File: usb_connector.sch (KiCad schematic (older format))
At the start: 7 parts

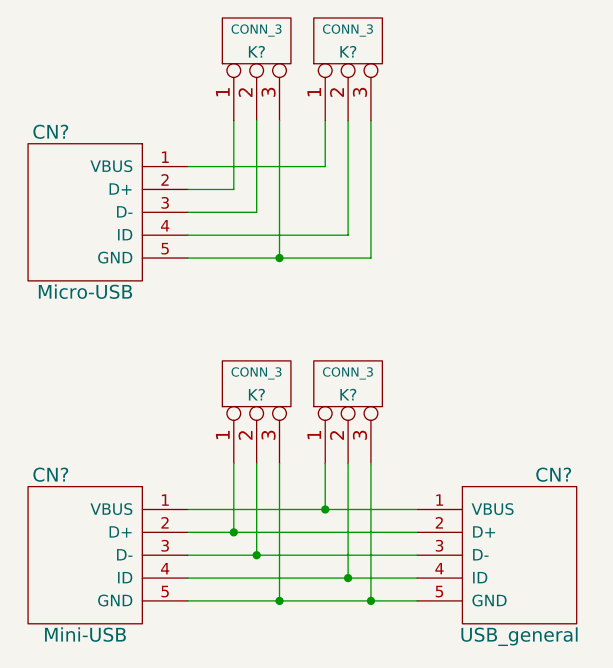
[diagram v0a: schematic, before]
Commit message: Add annotations to parts
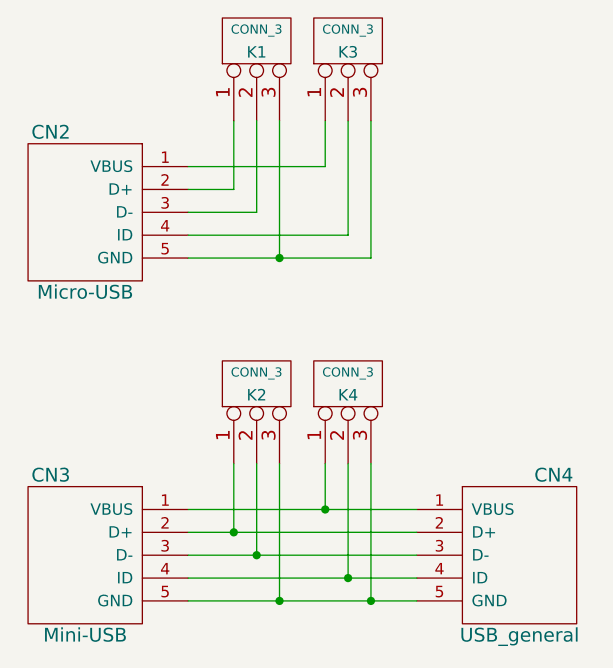
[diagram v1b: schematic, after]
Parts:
- gave numbers to parts that had none: 7
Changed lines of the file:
@@
 $EndDescr
 $Comp
-L USB_general CN?
+L USB_general CN3
 U 1 1 54E6FAE7
 P 3950 4750
-F 0 "CN?" H 3800 5100 60  0000 C CNN
+F 0 "CN3" H 3800 5100 60  0000 C CNN
 F 1 "Mini-USB" H 3950 4400 60  0000 C CNN
 F 2 "" H 4000 4650 60  0000 C CNN
@@
 $EndComp
 $Comp
-L USB_general CN?
+L USB_general CN2
 U 1 1 54E6FAEE
 P 3950 3250
-F 0 "CN?" H 3800 3600 60  0000 C CNN
+F 0 "CN2" H 3800 3600 60  0000 C CNN
 F 1 "Micro-USB" H 3950 2900 60  0000 C CNN
 F 2 "" H 4000 3150 60  0000 C CNN
@@
 	4400 4950 5400 4950
 $Comp
-L USB_general CN?
+L USB_general CN4
 U 1 1 54E6FAFA
 P 5850 4750
-F 0 "CN?" H 5700 5100 60  0000 C CNN
+F 0 "CN4" H 5700 5100 60  0000 C CNN
 F 1 "USB_general" H 5850 4400 60  0000 C CNN
 F 2 "" H 5900 4650 60  0000 C CNN
@@
 $EndComp
 $Comp
-L CONN_3 K?
+L CONN_3 K1
 U 1 1 54E6FB01
 P 4700 2500
-F 0 "K?" V 4650 2500 50  0000 C CNN
+F 0 "K1" V 4650 2500 50  0000 C CNN
 F 1 "CONN_3" V 4750 2500 40  0000 C CNN
 F 2 "" H 4700 2500 60  0000 C CNN
@@
 $EndComp
 $Comp
-L CONN_3 K?
+L CONN_3 K3
 U 1 1 54E6FB08
 P 5100 2500
-F 0 "K?" V 5050 2500 50  0000 C CNN
+F 0 "K3" V 5050 2500 50  0000 C CNN
 F 1 "CONN_3" V 5150 2500 40  0000 C CNN
 F 2 "" H 5100 2500 60  0000 C CNN
@@
 $EndComp
 $Comp
-L CONN_3 K?
+L CONN_3 K2
 U 1 1 54E6FB0F
 P 4700 4000
-F 0 "K?" V 4650 4000 50  0000 C CNN
+F 0 "K2" V 4650 4000 50  0000 C CNN
 F 1 "CONN_3" V 4750 4000 40  0000 C CNN
 F 2 "" H 4700 4000 60  0000 C CNN
@@
 $EndComp
 $Comp
-L CONN_3 K?
+L CONN_3 K4
 U 1 1 54E6FB16
 P 5100 4000
-F 0 "K?" V 5050 4000 50  0000 C CNN
+F 0 "K4" V 5050 4000 50  0000 C CNN
 F 1 "CONN_3" V 5150 4000 40  0000 C CNN
 F 2 "" H 5100 4000 60  0000 C CNN

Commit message: WT12 breakout headers are now in place
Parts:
- CN4: footprint (none) -> replacement_kinesis_controller:Pin_Header_Staggered_Straight_1x05
- K1, K2, K3, K4: footprint (none) -> replacement_kinesis_controller:Pin_Header_Staggered_Straight_1x03
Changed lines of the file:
@@
 F 0 "CN3" H 3800 5100 60  0000 C CNN
 F 1 "Mini-USB" H 3950 4400 60  0000 C CNN
-F 2 "" H 4000 4650 60  0000 C CNN
+F 2 "" H 4000 4650 60  0001 C CNN
 F 3 "" H 4000 4650 60  0000 C CNN
 	1    3950 4750
@@
 F 0 "CN2" H 3800 3600 60  0000 C CNN
 F 1 "Micro-USB" H 3950 2900 60  0000 C CNN
-F 2 "" H 4000 3150 60  0000 C CNN
+F 2 "" H 4000 3150 60  0001 C CNN
 F 3 "" H 4000 3150 60  0000 C CNN
 	1    3950 3250
@@
 F 0 "CN4" H 5700 5100 60  0000 C CNN
 F 1 "USB_general" H 5850 4400 60  0000 C CNN
-F 2 "" H 5900 4650 60  0000 C CNN
+F 2 "replacement_kinesis_controller:Pin_Header_Staggered_Straight_1x05" H 5900 4650 60  0001 C CNN
 F 3 "" H 5900 4650 60  0000 C CNN
 	1    5850 4750
@@
 F 0 "K1" V 4650 2500 50  0000 C CNN
 F 1 "CONN_3" V 4750 2500 40  0000 C CNN
-F 2 "" H 4700 2500 60  0000 C CNN
+F 2 "replacement_kinesis_controller:Pin_Header_Staggered_Straight_1x03" H 4700 2500 60  0001 C CNN
 F 3 "" H 4700 2500 60  0000 C CNN
 	1    4700 2500
@@
 F 0 "K3" V 5050 2500 50  0000 C CNN
 F 1 "CONN_3" V 5150 2500 40  0000 C CNN
-F 2 "" H 5100 2500 60  0000 C CNN
+F 2 "replacement_kinesis_controller:Pin_Header_Staggered_Straight_1x03" H 5100 2500 60  0001 C CNN
 F 3 "" H 5100 2500 60  0000 C CNN
 	1    5100 2500
@@
 F 0 "K2" V 4650 4000 50  0000 C CNN
 F 1 "CONN_3" V 4750 4000 40  0000 C CNN
-F 2 "" H 4700 4000 60  0000 C CNN
+F 2 "replacement_kinesis_controller:Pin_Header_Staggered_Straight_1x03" H 4700 4000 60  0001 C CNN
 F 3 "" H 4700 4000 60  0000 C CNN
 	1    4700 4000
@@
 F 0 "K4" V 5050 4000 50  0000 C CNN
 F 1 "CONN_3" V 5150 4000 40  0000 C CNN
-F 2 "" H 5100 4000 60  0000 C CNN
+F 2 "replacement_kinesis_controller:Pin_Header_Staggered_Straight_1x03" H 5100 4000 60  0001 C CNN
 F 3 "" H 5100 4000 60  0000 C CNN
 	1    5100 4000

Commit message: Add usb footprints
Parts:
- CN2: footprint (none) -> replacement_kinesis_controller:USB_micro_B-vertical
- CN3: footprint (none) -> replacement_kinesis_controller:USB_mini_B-vertical
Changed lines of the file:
@@
 F 0 "CN3" H 3800 5100 60  0000 C CNN
 F 1 "Mini-USB" H 3950 4400 60  0000 C CNN
-F 2 "" H 4000 4650 60  0001 C CNN
+F 2 "replacement_kinesis_controller:USB_mini_B-vertical" H 4000 4650 60  0001 C CNN
 F 3 "" H 4000 4650 60  0000 C CNN
 	1    3950 4750
@@
 F 0 "CN2" H 3800 3600 60  0000 C CNN
 F 1 "Micro-USB" H 3950 2900 60  0000 C CNN
-F 2 "" H 4000 3150 60  0001 C CNN
+F 2 "replacement_kinesis_controller:USB_micro_B-vertical" H 4000 3150 60  0001 C CNN
 F 3 "" H 4000 3150 60  0000 C CNN
 	1    3950 3250

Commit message: More traces laid
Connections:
- net at CN3.1 (VBUS), CN4.1 (VBUS): now also K2.2 (PM); no longer K4.1 (P1)
- net at CN3.2 (D+), CN4.2 (D+): now also K2.3 (P3); no longer K2.1 (P1)
- net at CN3.3 (D-), CN4.3 (D-): now also K4.2 (PM); no longer K2.2 (PM)
- net at CN3.4 (ID), CN4.4 (ID): now also K4.3 (P3); no longer K4.2 (PM)
- net at CN3.5 (GND), CN4.5 (GND): now also K2.1 (P1), K4.1 (P1); no longer K2.3 (P3), K4.3 (P3)
- net at CN2.1 (VBUS): now also K1.2 (PM); no longer K3.1 (P1)
- net at CN2.2 (D+): now also K1.3 (P3); no longer K1.1 (P1)
- net at CN2.3 (D-): now also K3.2 (PM); no longer K1.2 (PM)
- net at CN2.4 (ID): now also K3.3 (P3); no longer K3.2 (PM)
- new net: CN2.5 (GND), K1.1 (P1), K3.1 (P1)
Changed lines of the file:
@@
 $EndComp
 Wire Wire Line
-	4600 2850 4600 3150
+	4600 4350 4600 4950
+Connection ~ 4600 4950
 Wire Wire Line
-	4600 3150 4400 3150
+	4700 4350 4700 4550
+Connection ~ 4700 4550
 Wire Wire Line
-	4700 2850 4700 3250
+	4800 4350 4800 4650
+Connection ~ 4800 4650
 Wire Wire Line
-	4700 3250 4400 3250
+	5000 4350 5000 4950
+Connection ~ 5000 4950
 Wire Wire Line
-	4800 2850 4800 3450
+	5100 4350 5100 4750
+Connection ~ 5100 4750
 Wire Wire Line
-	4400 3450 5200 3450
+	5200 4350 5200 4850
+Connection ~ 5200 4850
 Wire Wire Line
-	5000 2850 5000 3050
+	4600 2850 4600 3450
 Wire Wire Line
-	5000 3050 4400 3050
+	4400 3450 5000 3450
 Wire Wire Line
-	5100 2850 5100 3350
+	4400 3050 4700 3050
 Wire Wire Line
-	5100 3350 4400 3350
+	4700 3050 4700 2850
 Wire Wire Line
-	5200 3450 5200 2850
-Connection ~ 4800 3450
+	4800 2850 4800 3150
 Wire Wire Line
-	4600 4350 4600 4650
-Connection ~ 4600 4650
+	4800 3150 4400 3150
 Wire Wire Line
-	4700 4350 4700 4750
-Connection ~ 4700 4750
+	5000 3450 5000 2850
+Connection ~ 4600 3450
 Wire Wire Line
-	4800 4350 4800 4950
-Connection ~ 4800 4950
+	5100 2850 5100 3250
 Wire Wire Line
-	5000 4350 5000 4550
-Connection ~ 5000 4550
+	5100 3250 4400 3250
 Wire Wire Line
-	5100 4350 5100 4850
-Connection ~ 5100 4850
+	5200 2850 5200 3350
 Wire Wire Line
-	5200 4350 5200 4950
-Connection ~ 5200 4950
+	5200 3350 4400 3350
 $EndSCHEMATC
